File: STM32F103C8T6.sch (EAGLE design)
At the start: 38 parts, among them IC1 MCP170333MB, J1 455-1750-1-ND, J2 455-1750-1-ND, J4 CORTEX_DEBUG_MINIMUM_PTH, U1 STM32F103C8T6

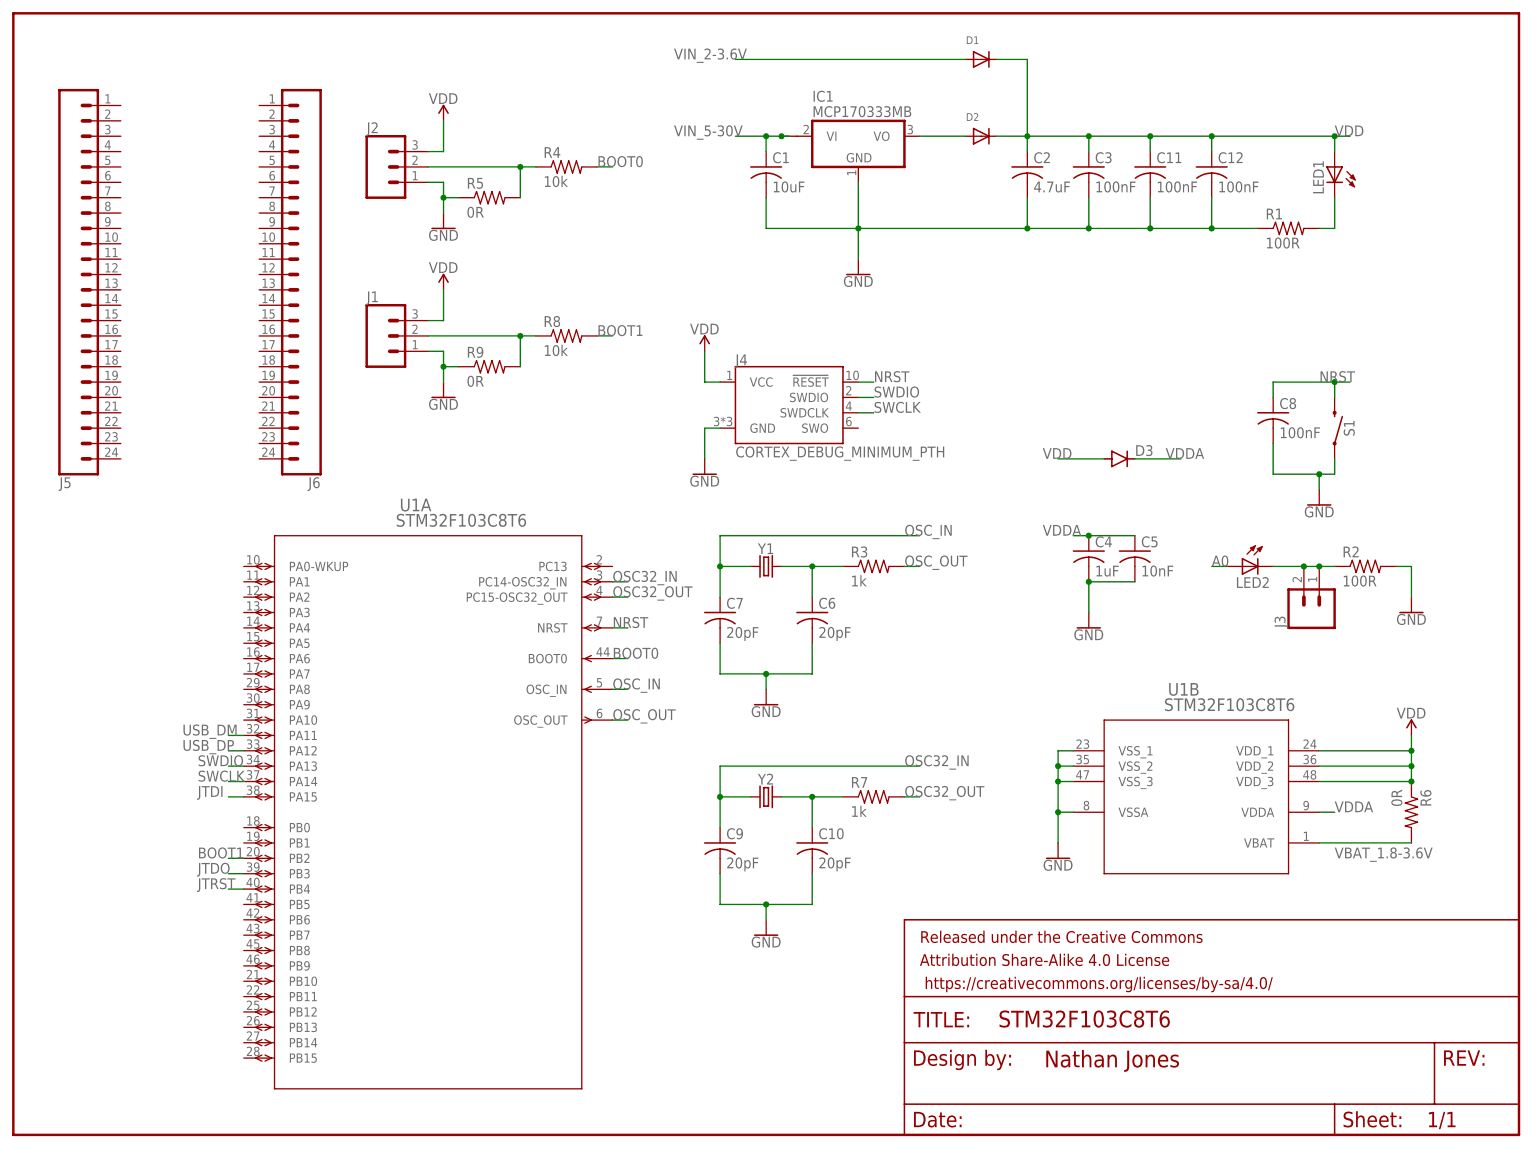
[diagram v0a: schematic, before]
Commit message: Added power capacitors. Added new LSE oscillator.
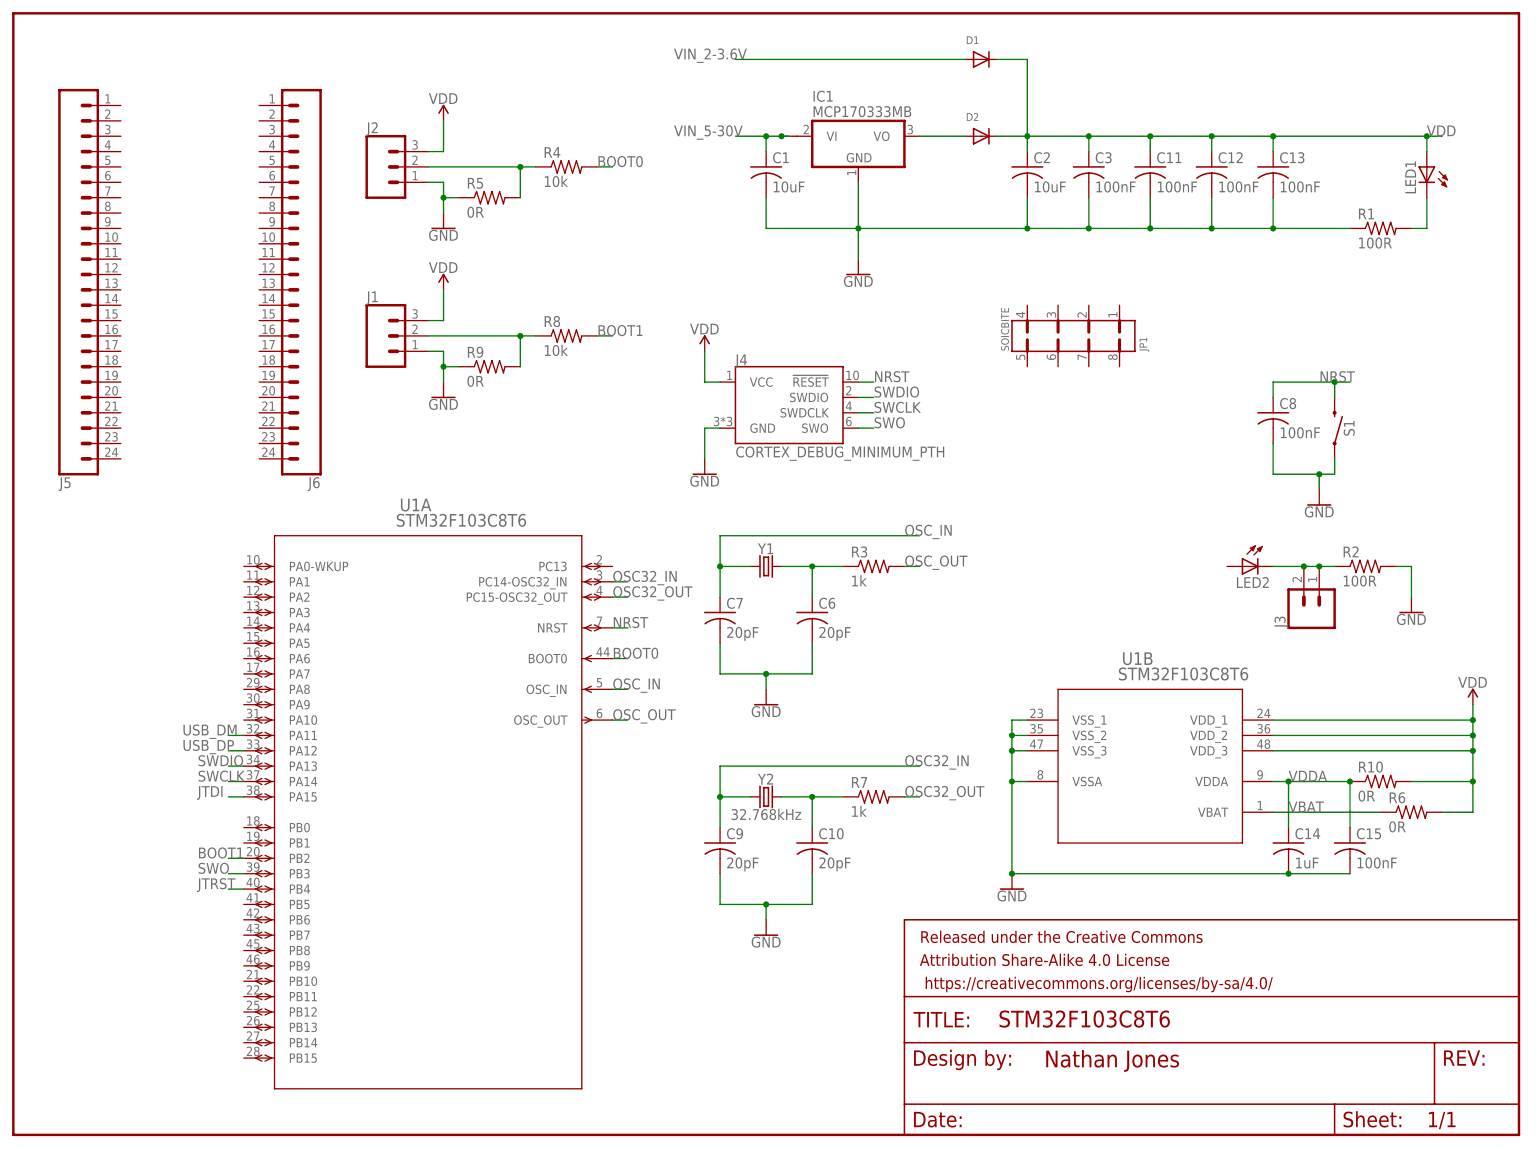
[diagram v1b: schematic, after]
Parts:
- removed C4: 1uF, adafruit:C-USC0603
- removed C5: 10nF, adafruit:C-USC0603
- removed D3: (no value), diode:DIODE-DO-214AC
- added C13, C15: 100nF, adafruit:C-USC0603
- added C14: 1uF, adafruit:C-USC0603
- added JP1: SOICBITE, SOICbite_Eagle:SOICBITE
- added R10: 0R, adafruit:R-US_R0603
- C2: value 4.7uF -> 10uF
- Y2: value (none) -> 32.768kHz; device SparkFun-Clocks:CRYSTALSMD-5X3.2-2PAD -> SparkFun-Clocks:CRYSTAL-32.768KHZSMD-3.2X1.5
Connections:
- removed net A0: LED2.A
- removed net JTDO: U1A.PB3
- removed net VBAT_1.8-3.6V: R6.2, U1B.VBAT
- new net SWO: J4.SWO, U1A.PB3
- new net VBAT: R6.1, U1B.VBAT
- net GND: now also C13.2, C14.2, C15.2; no longer C4.2, C5.2
- net N$4: now also Y2.2; no longer Y2.1
- net OSC32_IN: now also Y2.1; no longer Y2.2
- net VDD: now also C13.1, R10.2, R6.2; no longer D3.A, R6.1
- net VDDA: now also C14.1, C15.1, R10.1; no longer C4.1, C5.1, D3.C
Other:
- moved on the sheet: LED1, R1, R6, U1B

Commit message: Nearly finalized circuit.
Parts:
- removed C1, C2: 10uF, adafruit:C-USC0603
- removed C10, C6, C7, C9: 20pF, adafruit:C-USC0603
- removed C11, C12, C13, C15, C3, C8: 100nF, adafruit:C-USC0603
- removed C14: 1uF, adafruit:C-USC0603
- removed D1, D2: (no value), adafruit:DIODESOD-123
- removed IC1: MCP170333MB, linear:MCP170333MB
- removed JP1: SOICBITE, SOICbite_Eagle:SOICBITE
- removed R1: 100R, adafruit:R-US_R0603
- removed R10, R5, R6, R9: 0R, adafruit:R-US_R0603
- removed R3: 1k, adafruit:R-US_R0603
- removed R4, R8: 10k, adafruit:R-US_R0603
- added C16, C17, C18, C19, C25, C26: 100nF, adafruit:C-USC0402
- added C20, C21: 30pF, adafruit:C-USC0402
- added C22, C23: 15pF, adafruit:C-USC0402
- added C24: 1uF, adafruit:C-USC0402
- added C4, C5: 10uF, adafruit:C-USC0402
- added D3, D4: (no value), adafruit:DIODESOD-123
- added J7: AVX_009159010061916AVX_009159010061916_0_0, AVX - 009159010061916:AVX_009159010061916AVX_009159010061916_0_0
- added R12: 100R, adafruit:R-US_R0402
- added R13, R15: 10k, adafruit:R-US_R0402
- added R14, R16, R18: 0R, adafruit:R-US_R0402
- added R17: 680R, adafruit:R-US_R0402
- added U2: CJT1117-3.3-SOT223, OPL_IC:PMIC-CJT1117-3.3(SOT223)
- added USB1: 10118193-0001LF, OPL_Connector:MICRO-USB-SMD-B-(10118193-0001LF)
- J4: value CORTEX_DEBUG_MINIMUM_PTH -> (none); device SparkFun-Connectors:CORTEX_DEBUG_MINIMUM_PTH -> SparkFun-Connectors:CONN_02
- R7: value 1k -> 1k5; device adafruit:R-US_R0603 -> adafruit:R-US_R0402
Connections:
- removed net BOOT1: R8.2, U1A.PB2
- removed net JTDI: U1A.PA15
- removed net JTRST: U1A.PB4
- removed net N$4: C10.1, R7.1, Y2.2
- removed net N$5: D2.A, IC1.VO
- removed net SWCLK: J4.SWDCLK, U1A.PA14
- removed net SWDIO: J4.SWDIO, U1A.PA13
- removed net SWO: J4.SWO, U1A.PB3
- removed net USB_DM: U1A.PA11
- removed net USB_DP: U1A.PA12
- removed net VBAT: R6.1, U1B.VBAT
- removed net VDDA: C14.1, C15.1, R10.1, U1B.VDDA
- removed net VIN_2-3.6V: D1.A
- removed net VIN_5-30V: C1.1, IC1.VI1
- new net BOOT1*: R15.2, U1A.PB2
- new net JTDI*: J7.8, U1A.PA15
- new net JTRST*: J7.9, U1A.PB4
- new net PA0: U1A.PA0-WKUP
- new net PA1: U1A.PA1
- new net PA10*: U1A.PA10
- new net PA2: U1A.PA2
- new net PA3: U1A.PA3
- new net PA4: U1A.PA4
- new net PA5: U1A.PA5
- new net PA6: U1A.PA6
- new net PA7: U1A.PA7
- new net PA8*: U1A.PA8
- new net PA9*: U1A.PA9
- new net PB0: U1A.PB0
- new net PB1: U1A.PB1
- new net PB10*: U1A.PB10
- new net PB11*: U1A.PB11
- new net PB12*: U1A.PB12
- new net PB13*: U1A.PB13
- new net PB14*: U1A.PB14
- new net PB15*: U1A.PB15
- new net PB5: U1A.PB5
- new net PB6*: U1A.PB6
- new net PB7*: U1A.PB7
- new net PB8*: U1A.PB8
- new net PB9*: U1A.PB9
- new net PC13: U1A.PC13
- new net SWCLK*: J7.4, U1A.PA14
- new net SWDIO*: J7.2, U1A.PA13
- new net SWO*: J7.6, U1A.PB3
- new net USB_DM*: U1A.PA11, USB1.DM
- new net USB_DP*: R7.1, U1A.PA12, USB1.DP
- new net VBAT_1.8-3.6V: C26.1, R18.1, U1B.VBAT
- new net VIN: C4.1, D3.C, D4.C, U2.IN
- new net VIN_4.8-15V: D4.A
- new net VTREF: J7.1
- new net VUSB: D3.A, USB1.VCC
- net BOOT0: now also R13.2; no longer R4.2
- net GND: now also C16.2, C17.2, C18.2, C19.2, C20.2, C21.2, C22.2, C23.2, C24.2, C25.2, C26.2, C4.2, C5.2, J7.3, J7.5, R12.1, R14.1, R16.1, U2.GND, USB1.GND@1, USB1.GND@2, USB1.GND@3, USB1.GND@4, USB1.GND@5, USB1.ID; no longer C1.2, C10.2, C11.2, C12.2, C13.2, C14.2, C15.2, C2.2, C3.2, C6.2, C7.2, C8.2, C9.2, IC1.GND, J4.GND, R1.1, R5.1, R9.1
- net N$1: now also R13.1, R14.2; no longer R4.1, R5.2
- net N$3: now also C21.1, R17.1; no longer C6.1, R3.1
- net N$6: now also R15.1, R16.2; no longer R8.1, R9.2
- net N$7: now also R12.2; no longer R1.2
- net NRST: now also C19.1, J7.10; no longer C8.1, J4.!RESET
- net OSC32_IN: now also C22.1; no longer C9.1
- net OSC32_OUT: now also C23.1, Y2.2; no longer R7.2
- net OSC_IN: now also C20.1; no longer C7.1
- net OSC_OUT: now also R17.2; no longer R3.2
- net VDD: now also C16.1, C17.1, C18.1, C24.1, C25.1, C5.1, J4.1, J4.2, R18.2, R7.2, U1B.VDDA, U2.OUT; no longer C11.1, C12.1, C13.1, C2.1, C3.1, D1.C, D2.C, J4.VCC, R10.2, R6.2
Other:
- moved on the sheet: J1, J2, J3, J5, J6, LED1, LED2, R2, R7, S1, U1A, U1B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

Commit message: Nearly finished layout.
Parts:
- removed C17, C18: 100nF, adafruit:C-USC0402
- removed C20, C21: 30pF, adafruit:C-USC0402
- removed C22, C23: 15pF, adafruit:C-USC0402
- removed R12: 100R, adafruit:R-US_R0402
- removed R16, R18: 0R, adafruit:R-US_R0402
- removed R17: 680R, adafruit:R-US_R0402
- removed Y1: (no value), SparkFun-Clocks:CRYSTALSMD-5X3.2-2PAD
- removed Y2: 32.768kHz, SparkFun-Clocks:CRYSTAL-32.768KHZSMD-3.2X1.5
- added C1, C2: 10uF, adafruit:C-USC0402
- added C10: 0.1uF, adafruit:C-USC0402
- added C12: 01.uF, adafruit:C-USC0402
- added J8: (no value), SparkFun-Connectors:CONN_02
- added Q1, Q2: (no value), crystal-geyer_V1_0:KXO-VCXO-CMOS_4
- added R1: 1k5, adafruit:R-US_R0402
- added R8, R9: 100R, adafruit:R-US_R0402
- C4, C5: value 10uF -> 100nF
- J1, J2: value 455-1750-1-ND -> (none); device SparkFun-Connectors:CONN_03 -> SparkFun-Connectors:CONN_191X19_NO_SILK
- J3: value (none) -> AVX_009159010061916AVX_009159010061916_0_0; device SparkFun-Connectors:CONN_02 -> AVX - 009159010061916:AVX_009159010061916AVX_009159010061916_0_0
- J4: value (none) -> CORTEX_DEBUG_PTH; device SparkFun-Connectors:CONN_02 -> SparkFun-Connectors:CORTEX_DEBUG_PTH
- J5: device SparkFun-Connectors:CONN_24 -> SparkFun-Connectors:CONN_02
- J6: value (none) -> 455-1750-1-ND; device SparkFun-Connectors:CONN_24 -> SparkFun-Connectors:CONN_03
- J7: value AVX_009159010061916AVX_009159010061916_0_0 -> 455-1750-1-ND; device AVX - 009159010061916:AVX_009159010061916AVX_009159010061916_0_0 -> SparkFun-Connectors:CONN_03
- R2: value 100R -> 0R; device adafruit:R-US_R0603 -> adafruit:R-US_R0402
- R7: value 1k5 -> 0R
- U2: LCSC_PART (none) -> C6186
- renumbered C16 to C3, C19 to C9, C24 to C6, C25 to C7, C26 to C8, D3 to D1, D4 to D2, R13 to R4, R14 to R5, R15 to R6
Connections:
- removed net N$2: J3.1, J3.2, LED2.C, R2.1
- removed net N$3: C21.1, R17.1, Y1.1
- removed net VTREF: J7.1
- new net N$4: LED2.A, R9.2
- new net VREG: J5.2, U2.OUT
- net GND: now also C1.2, C10.2, C12.2, C2.2, J2.17, J3.8, J3.9, J4.GND@3, J4.GND@5, J6.1, J7.1, LED1.C, LED2.C, Q1.GND, Q2.GND, R7.1; no longer C17.2, C18.2, C20.2, C21.2, C22.2, C23.2, J1.1, J2.1, J7.3, J7.5, R12.1, R16.1, R2.2
- net JTDI*: now also J2.13, J3.2, J4.NC/TDI; no longer J7.8
- net JTRST*: now also J2.12, J3.6, J4.GNDDTCT; no longer J7.9
- net N$1: now also J6.2; no longer J2.2
- net N$6: now also J7.2, R7.2; no longer J1.2, R16.2
- net N$7: now also LED1.A, R8.1; no longer LED1.C, R12.2
- net NRST: now also J2.14, J3.1, J4.!RESET; no longer J7.10
- net OSC32_IN: now also Q2.OUT; no longer C22.1, Y2.1
- net OSC32_OUT: no longer C23.1, Y2.2
- net OSC_IN: now also Q1.OUT; no longer C20.1, Y1.2
- net OSC_OUT: no longer R17.2
- net PA0: now also J2.4
- net PA1: now also J2.3
- net PA10*: now also J1.16
- net PA2: now also J2.2
- net PA3: now also J2.1, J8.1, J8.2, R9.1
- net PA4: now also J1.1
- net PA5: now also J1.2
- net PA6: now also J1.3
- net PA7: now also J1.4
- net PA8*: now also J1.13
- net PA9*: now also J1.14
- net PB0: now also J1.5
- net PB1: now also J1.6
- net PB10*: now also J1.7
- net PB11*: now also J1.8
- net PB12*: now also J1.9
- net PB13*: now also J1.10
- net PB14*: now also J1.11
- net PB15*: now also J1.12
- net PB5: now also J2.11
- net PB6*: now also J2.10
- net PB7*: now also J2.9
- net PB8*: now also J2.8
- net PB9*: now also J2.7
- net PC13: now also J2.5
- net SWCLK*: now also J2.18, J3.4, J4.SWDCLK/TCK; no longer J7.4
- net SWDIO*: now also J2.16, J3.5, J4.SWDIO/TMS; no longer J7.2
- net SWO*: now also J2.15, J3.3, J4.SWO/TDO; no longer J7.6
- net USB_DM*: now also J1.17
- net USB_DP*: now also J1.18, R1.1; no longer R7.1
- net VBAT_1.8-3.6V: now also J2.6, R2.1; no longer R18.1
- net VDD: now also C10.1, C12.1, C2.1, C4.1, J2.19, J3.10, J4.VCC, J5.1, J6.3, J7.3, Q1.VDD, Q2.VDD, R1.2, R2.2, R8.2; no longer C17.1, C18.1, J1.3, J2.3, J4.1, J4.2, LED1.A, R18.2, R7.2, U2.OUT
- net VIN: now also C1.1; no longer C4.1
- net VIN_4.8-15V: now also J1.15
- net VUSB: now also J1.19
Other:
- moved on the sheet: C4, C5, LED1, LED2, R2, R7

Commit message: Finished layout.
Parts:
- removed C12: 01.uF, adafruit:C-USC0402
- removed R9: 100R, adafruit:R-US_R0402
- removed USB1: 10118193-0001LF, OPL_Connector:MICRO-USB-SMD-B-(10118193-0001LF)
- added C11: 100nF, adafruit:C-USC0402
- added R3: 10k, adafruit:R-US_R0402
- C1, C2: LCSC_PART (none) -> C15525
- C10: value 0.1uF -> 100nF; LCSC_PART (none) -> C1525
- C3, C4, C5, C7, C8, C9: LCSC_PART (none) -> C1525
- C6: LCSC_PART (none) -> C52923
- D1, D2: LCSC_PART (none) -> C8598
- J3: value AVX_009159010061916AVX_009159010061916_0_0 -> AVX_6-PIN_009159006061916; device AVX - 009159010061916:AVX_009159010061916AVX_009159010061916_0_0 -> Debug-Edge_AVX-connectors:AVX_6-PIN_009159006061916
- J5: value (none) -> 10118194-0001LF; device SparkFun-Connectors:CONN_02 -> USB-micro-B_Amphenol_10118194-0001LF:10118194-0001LF
- J6, J7: value 455-1750-1-ND -> (none); device SparkFun-Connectors:CONN_03 -> SparkFun-Connectors:CONN_031X03_NO_SILK
- J8: device SparkFun-Connectors:CONN_02 -> SparkFun-Connectors:CONN_021X02_NO_SILK
- LED1: LCSC_PART (none) -> C72041
- LED2: LCSC_PART (none) -> C72038
- R1: LCSC_PART (none) -> C25867
- R2: LCSC_PART (none) -> C17168
- R4, R6: value 10k -> 0R; LCSC_PART (none) -> C17168
- R5: value 0R -> 10k; LCSC_PART (none) -> C25744
- R7: value 0R -> 150R; LCSC_PART (none) -> C25082
- R8: value 100R -> 150R; LCSC_PART (none) -> C25082
- S1: LCSC_PART (none) -> C318884
- U1: LCSC_PART (none) -> C94046
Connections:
- removed net VREG: J5.2, U2.OUT
- net BOOT0: now also R3.2; no longer R4.2
- net BOOT1*: now also R5.2; no longer R6.2
- net GND: now also C11.2, J3.6, J5.4, J5.5, R4.1, R6.1; no longer C12.2, J3.8, J3.9, R5.1, R7.1, USB1.GND@1, USB1.GND@2, USB1.GND@3, USB1.GND@4, USB1.GND@5, USB1.ID
- net JTDI*: no longer J3.2
- net JTRST*: no longer J3.6
- net N$1: now also R3.1, R4.2; no longer R4.1, R5.2
- net N$4: now also R8.2; no longer R9.2
- net N$6: now also R5.1, R6.2; no longer R6.1, R7.2
- net N$7: now also R7.1; no longer R8.1
- net NRST: now also J3.5; no longer J3.1
- net PA10*: now also J1.15; no longer J1.16
- net PA3: now also R8.1; no longer R9.1
- net SWCLK*: now also J3.2; no longer J3.4
- net SWDIO*: now also J3.1; no longer J3.5
- net USB_DM*: now also J5.2; no longer USB1.DM
- net USB_DP*: now also J5.3; no longer USB1.DP
- net VDD: now also C11.1, J3.4, R7.2, U2.OUT; no longer C12.1, J3.10, J5.1, R8.2
- net VIN_4.8-15V: now also J1.16; no longer J1.15
- net VUSB: now also J5.1; no longer USB1.VCC
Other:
- note added: "BOOT0/BOOT1"
- note added: "Ext. Oscillators"
- note added: "J-Link Connectors"
- note added: "MCU"
- note added: "Power"
- note added: "Reset"
- note added: "User LED"
- moved on the sheet: C1, C10, C2, C3, C4, C5, C6, C7, C8, C9, D1, D2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
